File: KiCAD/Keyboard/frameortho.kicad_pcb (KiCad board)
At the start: 2 copper layers, 276 x 105 mm, 122 parts, among them SW1 SW_Push, SW2 SW_Push, U1 RP2040, U2 W25Q128JVS, U3 XC6206PxxxMR, Y1 12 MHz 20pF

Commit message: update some stuff
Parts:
- moved TP17 12.2 mm to (218.3, 83.2), turned to -90 degrees
- moved TP20 12.1 mm to (206.2, 83.2), turned to -90 degrees
- moved TP18 4.06 mm to (214.3, 83.2), turned to -90 degrees
- moved TP19 4.04 mm to (210.2, 83.2), turned to -90 degrees
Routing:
- net GND: track 86.6 -> 100.0 mm
- net +5V: track 20.4 -> 8.57 mm
- net COL_0: track 162.5 -> 160.1 mm
- net D_N: track 26.3 -> 27.0 mm

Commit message: idk what i did tbh
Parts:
- turned TP20 to 90 degrees
- turned TP18 to 90 degrees
- turned TP19 to 90 degrees
- turned TP17 to 90 degrees
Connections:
- U1 pad 27: COL_9 -> GPIO16
- U1 pad 28: COL_8 -> GPIO17
- U1 pad 29: COL_7 -> GPIO18
- U1 pad 30: COL_6 -> GPIO19
- U1 pad 31: COL_5 -> GPIO20
- U1 pad 32: GPIO21 -> COL_9
- U1 pad 34: GPIO22 -> COL_8
- U1 pad 35: GPIO23 -> COL_7
- U1 pad 36: GPIO24 -> COL_6
- U1 pad 37: GPIO25 -> COL_5
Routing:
- net GPIO23: track 57.2 -> 51.7 mm
- net GPIO21: track 45.9 -> 40.6 mm, vias 4 -> 2
- net GPIO24: track 54.3 -> 49.5 mm
- net GPIO22: track 59.8 -> 55.1 mm
- net GPIO25: track 53.5 -> 49.2 mm
- net COL_9: track 133.7 -> 131.9 mm
- net COL_8: track 114.7 -> 112.9 mm
- net GND: track 100.0 -> 98.4 mm
- net COL_5: track 113.2 -> 114.1 mm
- net COL_6: track 133.9 -> 134.4 mm
- net SWDIO: track 28.9 -> 28.6 mm, vias 4 -> 2
- net SWCLK: track 26.1 -> 25.9 mm, vias 4 -> 2
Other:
- board text removed: "5V"
- board text removed: "D+"
- board text removed: "D-"
- board text removed: "GND"

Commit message: why no commit
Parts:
- added 1.1V: TestPoint, TestPoint:TestPoint_Pad_D2.0mm, F.Cu at (221.1, 99.1)
- added 3.3V: TestPoint, TestPoint:TestPoint_Pad_D2.0mm, F.Cu at (221.1, 103.1)
- added C16: 1µF, Capacitor_SMD:C_0402_1005Metric, F.Cu at (216.9, 89.4)
- added C17: 100nF, Capacitor_SMD:C_0402_1005Metric, F.Cu at (219.0, 103.6)
- added C18: 100nF, Capacitor_SMD:C_0402_1005Metric, F.Cu at (219.2, 99.6)
- added GND: TestPoint, TestPoint:TestPoint_Pad_D2.0mm, F.Cu at (221.1, 107.2)
- C14, C15: value 33pF -> 27pF
- Y1: value 12 MHz 20pF -> 12 MHz 18pF
- moved TP18 4.06 mm to (210.3, 83.2), turned to -90 degrees
- moved TP19 4.04 mm to (214.3, 83.2), turned to -90 degrees
- moved C11 0.73 mm to (215.8, 107.9)
- moved C2 0.73 mm to (216.8, 107.9)
- moved R3 0.41 mm to (213.3, 108.2)
- moved R4 0.41 mm to (214.4, 108.2)
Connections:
- TP12 pad 1: GPIO21 -> GPIO16
- TP13 pad 1: GPIO22 -> GPIO17
- TP14 pad 1: GPIO23 -> GPIO18
- TP15 pad 1: GPIO24 -> GPIO19
- TP16 pad 1: GPIO25 -> GPIO20
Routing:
- net GPIO22: track 55.1 -> 0.00 mm, vias 2 -> 0
- net GPIO17: track 0.00 -> 55.1 mm, vias 0 -> 2
- net GPIO23: track 51.7 -> 0.00 mm, vias 2 -> 0
- net GPIO18: track 0.00 -> 51.7 mm, vias 0 -> 2
- net GPIO24: track 49.5 -> 0.00 mm, vias 2 -> 0
- net GPIO19: track 0.00 -> 49.5 mm, vias 0 -> 2
- net GPIO25: track 49.2 -> 0.00 mm, vias 2 -> 0
- net GPIO20: track 0.00 -> 49.2 mm, vias 0 -> 2
- net GPIO21: track 40.6 -> 0.00 mm, vias 2 -> 0
- net GPIO16: track 0.00 -> 40.6 mm, vias 0 -> 2
- net +1V1: track 30.0 -> 45.1 mm, vias 3 -> 5
- net GND: track 98.4 -> 112.6 mm, vias 26 -> 37
- net +3V3: track 112.4 -> 120.8 mm
- net COL_6: track 134.4 -> 136.9 mm
- net COL_5: track 114.1 -> 116.5 mm
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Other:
- board text added: "5V"
- board text added: "D+"
- board text added: "D-"
- board text added: "GND"
- board text added: "GPIO17"
- board text added: "GPIO18"
- board text added: "GPIO19"
- board text added: "GPIO20"
- board text removed: "GPIO22"
- board text removed: "GPIO23"
- board text removed: "GPIO24"
- board text removed: "GPIO25"

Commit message: whatever
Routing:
- net GND: track 112.6 -> 108.9 mm, vias 37 -> 38
- net GPIO17: track 55.1 -> 56.1 mm
- net GPIO19: track 49.5 -> 50.5 mm
- net GPIO18: track 51.7 -> 52.7 mm

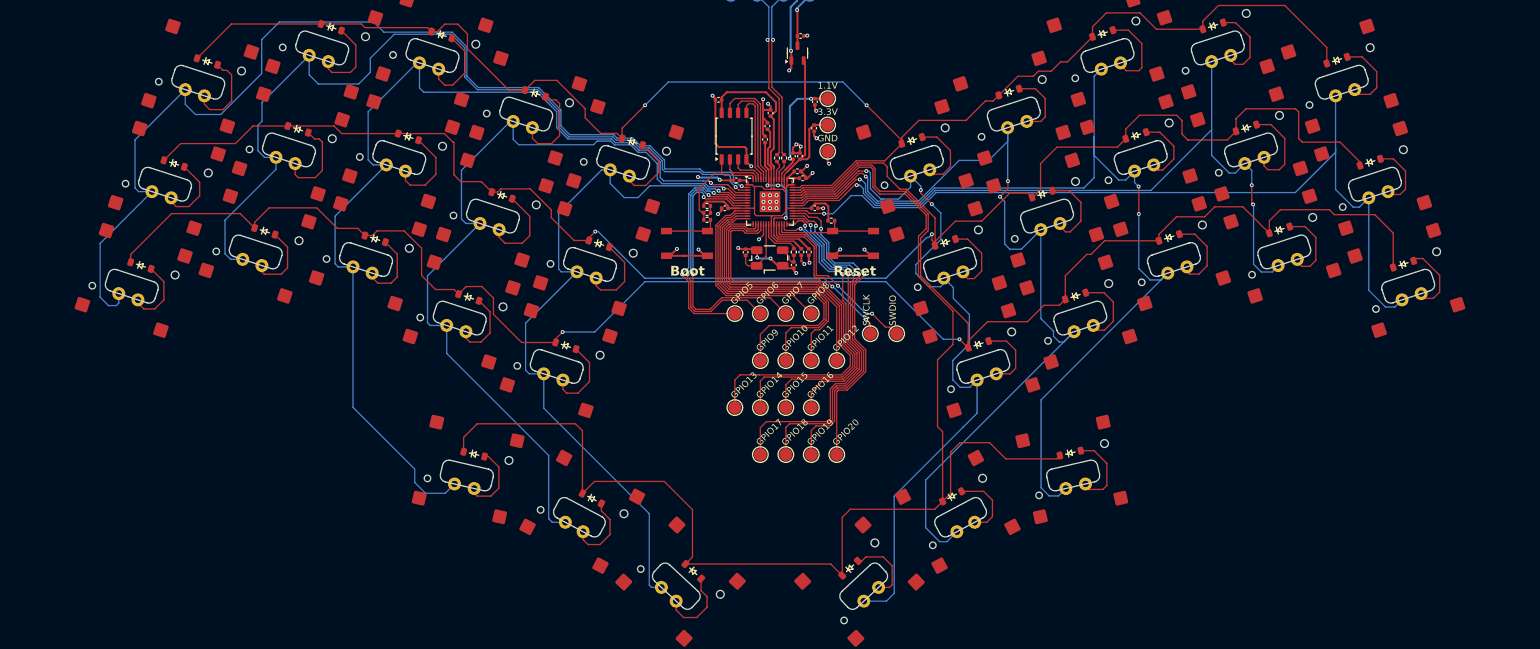
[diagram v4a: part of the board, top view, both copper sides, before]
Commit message: mounting holes
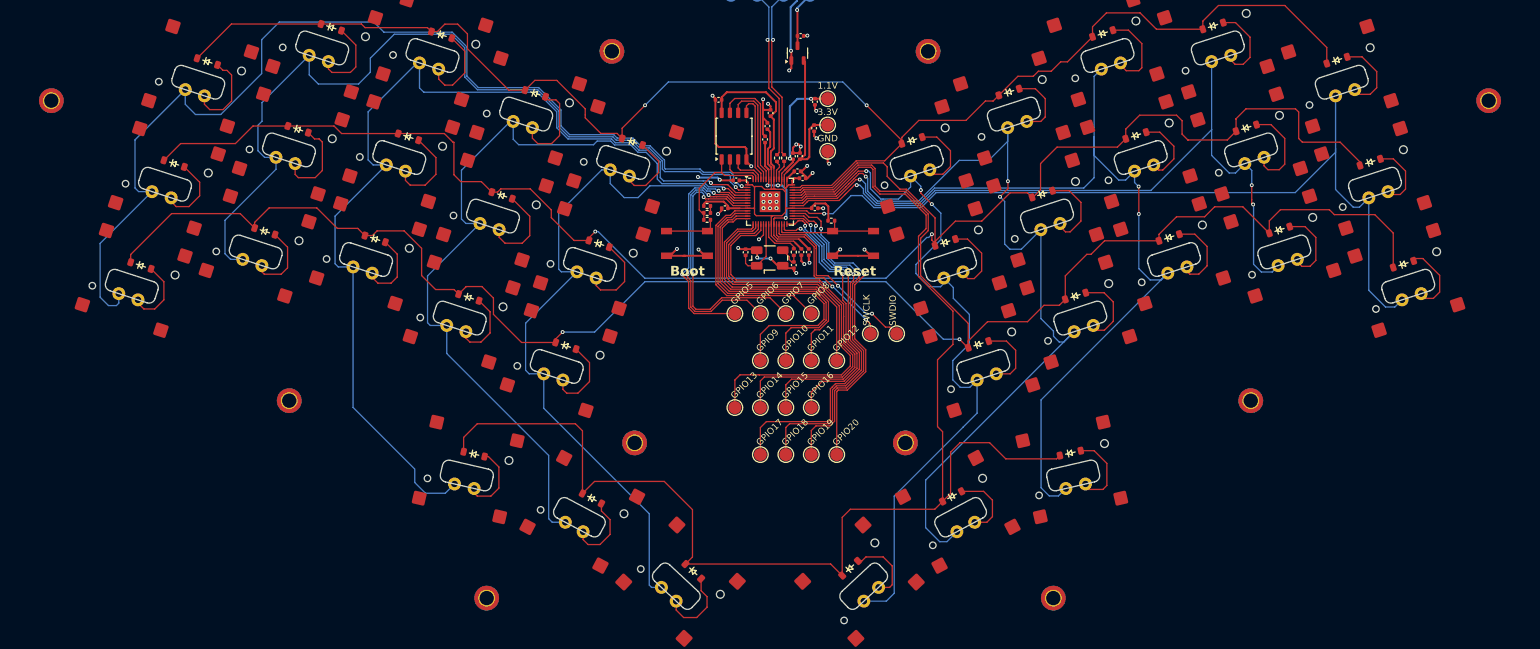
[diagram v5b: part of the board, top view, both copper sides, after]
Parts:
- added H1: MountingHole_Pad, MountingHole:MountingHole_2.2mm_M2_DIN965_Pad_TopBottom, F.Cu at (191.4, 152.0)
- added H10: MountingHole_Pad, MountingHole:MountingHole_2.2mm_M2_DIN965_Pad_TopBottom, F.Cu at (255.8, 175.9)
- added H2: MountingHole_Pad, MountingHole:MountingHole_2.2mm_M2_DIN965_Pad_TopBottom, F.Cu at (187.9, 91.8)
- added H3: MountingHole_Pad, MountingHole:MountingHole_2.2mm_M2_DIN965_Pad_TopBottom, F.Cu at (233.1, 152.0)
- added H4: MountingHole_Pad, MountingHole:MountingHole_2.2mm_M2_DIN965_Pad_TopBottom, F.Cu at (236.6, 91.8)
- added H5: MountingHole_Pad, MountingHole:MountingHole_2.2mm_M2_DIN965_Pad_TopBottom, F.Cu at (138.3, 145.5)
- added H6: MountingHole_Pad, MountingHole:MountingHole_2.2mm_M2_DIN965_Pad_TopBottom, F.Cu at (101.7, 99.4)
- added H7: MountingHole_Pad, MountingHole:MountingHole_2.2mm_M2_DIN965_Pad_TopBottom, F.Cu at (286.2, 145.5)
- added H8: MountingHole_Pad, MountingHole:MountingHole_2.2mm_M2_DIN965_Pad_TopBottom, F.Cu at (322.8, 99.4)
- added H9: MountingHole_Pad, MountingHole:MountingHole_2.2mm_M2_DIN965_Pad_TopBottom, F.Cu at (168.7, 175.9)
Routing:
- net GPIO15: track 57.9 -> 56.0 mm
- net GPIO14: track 61.7 -> 59.8 mm
- net GPIO13: track 65.1 -> 63.4 mm
- net GPIO12: track 40.0 -> 38.9 mm
